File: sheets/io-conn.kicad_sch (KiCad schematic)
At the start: 2 parts, among them J10 Conn_02x05_Odd_Even, SW10 TDS08SGRNTU04

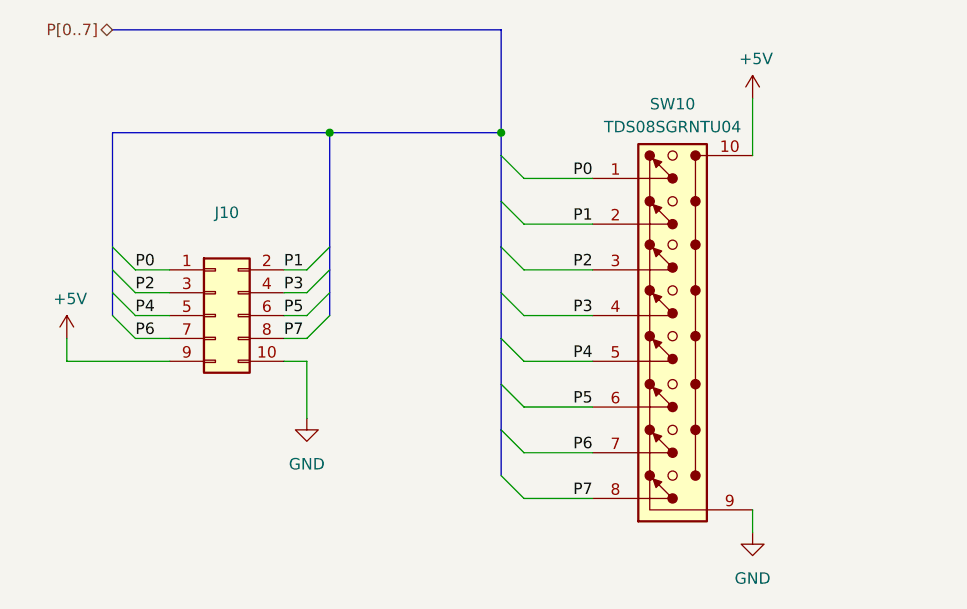
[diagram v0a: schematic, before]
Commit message: updated silk + started routing
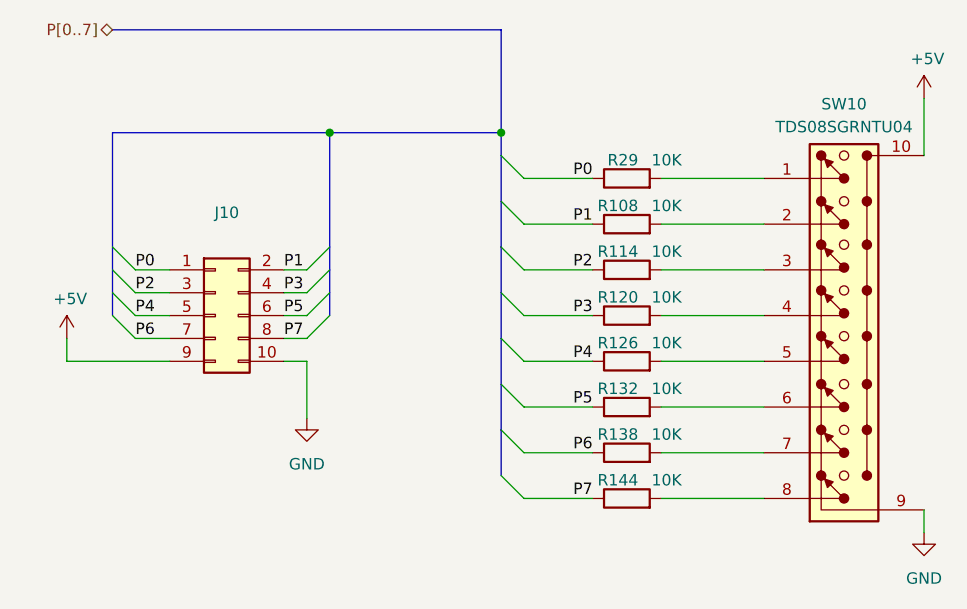
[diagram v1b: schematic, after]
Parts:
- added R108, R114, R120, R126, R132, R138, R144, R29: 10K, Resistor_SMD:R_0603_1608Metric, symbol Device:R
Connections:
- net P0: now also R29.1; no longer SW10.1
- net P1: now also R108.1; no longer SW10.2
- net P2: now also R114.1; no longer SW10.3
- net P3: now also R120.1; no longer SW10.4
- net P4: now also R126.1; no longer SW10.5
- net P5: now also R132.1; no longer SW10.6
- net P6: now also R138.1; no longer SW10.7
- net P7: now also R144.1; no longer SW10.8
- new net: R108.2, SW10.2
- new net: R126.2, SW10.5
- new net: R29.2, SW10.1
- new net: R114.2, SW10.3
- new net: R120.2, SW10.4
- new net: R132.2, SW10.6
- new net: R138.2, SW10.7
- new net: R144.2, SW10.8
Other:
- moved on the sheet: SW10
